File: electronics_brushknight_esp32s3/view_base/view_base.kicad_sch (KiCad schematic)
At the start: 108 parts, among them J1 BLDC, J2 USB_C_Receptacle_USB2.0, J3 LCD, J4 A, J5 B, J6 LCD - FPC, Q1 MMBT4403, Q2 UMH3N, U1 MT6701-CT, U10 ESP32-S3-WROOM-1-N8R8, U4 CP2102N-A02-GQFN28, U4 HX711, U5 TMC6300, U7 SN74LV1T34DBV, U8 VEML7700, U9 TS1117BCW33_RPG

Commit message: re-routed things
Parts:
- removed D1, D2, D3, D4, D5, D6, D7, D8: SK6812SIDE-A, cleaned footprints:SK6812-SIDE-A, symbol SK6812:SK6812SIDE-A
- removed H4: MountHole, Holes:MountingHole_2.2mm_M2_ISO7380_Pad_NonVirtual, symbol Mechanical:MountingHole_Pad
- removed Q2: UMH3N, cleaned footprints:SOT-363_SC-70-6, symbol Transistor_BJT:UMH3N
- removed R3: 1K, cleaned footprints:R_0603_1608Metric, symbol Device:R_Small
- removed U4: CP2102N-A02-GQFN28, cp2102:Silicon_Labs-CP2102N-A02-GQFN28-IPC_A, symbol terrarium-rescue:CP2102N-A02-GQFN28-CP2102N-A02-GQFN28
- added C100, C101, C30, C31, C32, C33, C34, C35, C36, C37, C38, C39, C40, C41, C42, C43, C44, C45, C46, C47, C48, C49, C50, C51, C52, C53, C54, C55, C56, C57, C58, C59, C60, C61, C62, C63, C64, C65, C66, C67, C68, C69, C70, C71, C72, C73, C74, C75, C76, C77, C79, C80, C81, C82, C88, C90, C92, C94, C95, C96, C97, C98, C99: 0.1uF, cleaned footprints:C_0402_1005Metric, symbol Device:C_Small
- added C27, C38: 10uF, smd_clean:C_0603_1608Metric, symbol Device:C_Small
- added C39: 100nF, smd_clean:C_0603_1608Metric, symbol Device:C_Small
- added D10, D11, D12, D13, D14, D15, D16, D17, D18, D19, D20, D21, D22, D23, D24, D25, D26, D27, D28, D29, D30, D31, D32, D33, D34, D35, D36, D37, D38, D39, D40, D41, D42, D43, D44, D45, D46, D47, D48, D49, D50, D51, D52, D53, D54, D55, D56, D57, D58, D59, D60, D61, D62, D63, D64, D65, D66, D67, D68, D69, D70, D71, D72, D73, D74, D75, D76, D77, D78, D79, D80, D9: SK6812, cleaned footprints:LED_SK6812_EC15_1.5x1.5mm, symbol LED:SK6812
- added Q4, Q5: BSS138, smd_clean:SOT-23, symbol Transistor_FET:BSS138
- added R18, R19, R20, R21, R22, R23: 10K, smd_clean:R_0603_1608Metric, symbol Device:R_Small
- added U2: USBLC6-2SC6, Package_TO_SOT_SMD:SOT-23-6, symbol Power_Protection:USBLC6-2SC6
- added U7: VL53L0CXV0DH_1, smd_clean:LGA12_1, symbol VL53L0CXV0DH_1:VL53L0CXV0DH_1
- added U8: LP5907MFX-2.8, Package_TO_SOT_SMD:SOT-23-5, symbol Regulator_Linear:LP5907MFX-2.8
- C1, C11, C2, C29, C3, C4, C5, C6, C7, C8: footprint cleaned footprints:C_0603_1608Metric -> cleaned footprints:C_0402_1005Metric
- TP1, TP10, TP11, TP12, TP13, TP14, TP15, TP16, TP3, TP4, TP5, TP6, TP7, TP8, TP9: footprint Modified:TestPoint_Pad_D2.0mm_ValueSilk -> cleaned footprints:TestPoint_Pad_D2.0mm_ValueSilk
- TP2: value 3.3v -> 3V3; footprint Modified:TestPoint_Pad_D2.0mm_ValueSilk -> cleaned footprints:TestPoint_Pad_D2.0mm_ValueSilk
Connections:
- net +3V3: now also C27.2, R20.2, R21.2, U8.1 (IN), U8.3 (EN); no longer C11.1
- net +5V: now also C11.1, C100.1, C101.1, C30.1, C31.1, C32.1, C33.1, C34.1, C35.1, C36.1, C37.1, C38.1, C39.1, C40.1, C41.1, C42.1, C43.1, C44.1, C45.1, C46.1, C47.1, C48.1, C49.1, C50.1, C51.1, C52.1, C53.1, C54.1, C55.1, C56.1, C57.1, C58.1, C59.1, C60.1, C61.1, C62.1, C63.1, C64.1, C65.1, C66.1, C67.1, C68.1, C69.1, C70.1, C71.1, C72.1, C73.1, C74.1, C75.1, C76.1, C77.1, C79.1, C80.1, C81.1, C82.1, C88.1, C90.1, C92.1, C94.1, C95.1, C96.1, C97.1, C98.1, C99.1, D10.3 (VDD), D11.3 (VDD), D12.3 (VDD), D13.3 (VDD), D14.3 (VDD), D15.3 (VDD), D16.3 (VDD), D17.3 (VDD), D18.3 (VDD), D19.3 (VDD), D20.3 (VDD), D21.3 (VDD), D22.3 (VDD), D23.3 (VDD), D24.3 (VDD), D25.3 (VDD), D26.3 (VDD), D27.3 (VDD), D28.3 (VDD), D29.3 (VDD), D30.3 (VDD), D31.3 (VDD), D32.3 (VDD), D33.3 (VDD), D34.3 (VDD), D35.3 (VDD), D36.3 (VDD), D37.3 (VDD), D38.3 (VDD), D39.3 (VDD), D40.3 (VDD), D41.3 (VDD), D42.3 (VDD), D43.3 (VDD), D44.3 (VDD), D45.3 (VDD), D46.3 (VDD), D47.3 (VDD), D48.3 (VDD), D49.3 (VDD), D50.3 (VDD), D51.3 (VDD), D52.3 (VDD), D53.3 (VDD), D54.3 (VDD), D55.3 (VDD), D56.3 (VDD), D57.3 (VDD), D58.3 (VDD), D59.3 (VDD), D60.3 (VDD), D61.3 (VDD), D62.3 (VDD), D63.3 (VDD), D64.3 (VDD), D65.3 (VDD), D66.3 (VDD), D67.3 (VDD), D68.3 (VDD), D69.3 (VDD), D70.3 (VDD), D71.3 (VDD), D72.3 (VDD), D73.3 (VDD), D74.3 (VDD), D75.3 (VDD), D76.3 (VDD), D77.3 (VDD), D78.3 (VDD), D79.3 (VDD), D80.3 (VDD), D9.3 (VDD), U2.5 (VBUS)
- net GND: now also C100.2, C101.2, C27.1, C30.2, C31.2, C32.2, C33.2, C34.2, C35.2, C36.2, C37.2, C38.1, C38.2, C39.1, C39.2, C40.2, C41.2, C42.2, C43.2, C44.2, C45.2, C46.2, C47.2, C48.2, C49.2, C50.2, C51.2, C52.2, C53.2, C54.2, C55.2, C56.2, C57.2, C58.2, C59.2, C60.2, C61.2, C62.2, C63.2, C64.2, C65.2, C66.2, C67.2, C68.2, C69.2, C70.2, C71.2, C72.2, C73.2, C74.2, C75.2, C76.2, C77.2, C79.2, C80.2, C81.2, C82.2, C88.2, C90.2, C92.2, C94.2, C95.2, C96.2, C97.2, C98.2, C99.2, D10.1 (VSS), D11.1 (VSS), D12.1 (VSS), D13.1 (VSS), D14.1 (VSS), D15.1 (VSS), D16.1 (VSS), D17.1 (VSS), D18.1 (VSS), D19.1 (VSS), D20.1 (VSS), D21.1 (VSS), D22.1 (VSS), D23.1 (VSS), D24.1 (VSS), D25.1 (VSS), D26.1 (VSS), D27.1 (VSS), D28.1 (VSS), D29.1 (VSS), D30.1 (VSS), D31.1 (VSS), D32.1 (VSS), D33.1 (VSS), D34.1 (VSS), D35.1 (VSS), D36.1 (VSS), D37.1 (VSS), D38.1 (VSS), D39.1 (VSS), D40.1 (VSS), D41.1 (VSS), D42.1 (VSS), D43.1 (VSS), D44.1 (VSS), D45.1 (VSS), D46.1 (VSS), D47.1 (VSS), D48.1 (VSS), D49.1 (VSS), D50.1 (VSS), D51.1 (VSS), D52.1 (VSS), D53.1 (VSS), D54.1 (VSS), D55.1 (VSS), D56.1 (VSS), D57.1 (VSS), D58.1 (VSS), D59.1 (VSS), D60.1 (VSS), D61.1 (VSS), D62.1 (VSS), D63.1 (VSS), D64.1 (VSS), D65.1 (VSS), D66.1 (VSS), D67.1 (VSS), D68.1 (VSS), D69.1 (VSS), D70.1 (VSS), D71.1 (VSS), D72.1 (VSS), D73.1 (VSS), D74.1 (VSS), D75.1 (VSS), D76.1 (VSS), D77.1 (VSS), D78.1 (VSS), D79.1 (VSS), D80.1 (VSS), D9.1 (VSS), U2.2 (GND), U7.12 (GND4), U7.2 (AVSSVCSEL), U7.3 (GND), U7.4 (GND2), U7.6 (GND3), U8.2 (GND)
- net LCD_RST: now also U10.18 (IO10); no longer U10.6 (IO6)
- net LED_DATA_3V3: now also U10.20 (IO12); no longer U10.7 (IO7)
- net LED_DATA_5V: now also D9.2 (DIN)
- net MAG_CSN: now also U10.19 (IO11); no longer U10.22 (IO14)
- net MAG_DO: now also U10.22 (IO14); no longer U10.30 (IO37)
- net SCL: now also U10.31 (IO38), Q4.3 (D), R21.1; no longer U10.12 (IO8)
- net SDA: now also U10.32 (IO39), Q5.3 (D), R20.1; no longer U10.8 (IO15)
- net STRAIN_DO: now also U10.23 (IO21); no longer U10.31 (IO38)
- net TMC_DIAG: now also U10.6 (IO6); no longer U10.29 (IO36)
- net TMC_UH: now also U10.12 (IO8); no longer U10.14 (IO20)
- net TMC_UL: now also U10.9 (IO16); no longer U10.13 (IO19)
- net TMC_VH: now also U10.11 (IO18); no longer U10.23 (IO21)
- net TMC_VL: now also U10.7 (IO7); no longer U10.10 (IO17)
- net TMC_WH: now also U10.10 (IO17); no longer U10.20 (IO12)
- net TMC_WL: now also U10.8 (IO15); no longer U10.11 (IO18)
- net USB_D+: now also U2.3 (I/O2)
- net USB_D-: now also U2.1 (I/O1)
- new net: D27.4 (DOUT), D28.2 (DIN)
- new net: D28.4 (DOUT), D29.2 (DIN)
- new net: D19.4 (DOUT), D20.2 (DIN)
- new net: D20.4 (DOUT), D21.2 (DIN)
- new net: D16.4 (DOUT), D17.2 (DIN)
- new net: D17.4 (DOUT), D18.2 (DIN)
- new net: D34.4 (DOUT), D35.2 (DIN)
- new net: D35.4 (DOUT), D36.2 (DIN)
- new net: D36.4 (DOUT), D37.2 (DIN)
- new net: R19.1, U7.7 (GPIO1)
- new net: D48.4 (DOUT), D52.2 (DIN)
- new net: D52.4 (DOUT), D56.2 (DIN)
- new net: D59.4 (DOUT), D63.2 (DIN)
- new net: D63.4 (DOUT), D67.2 (DIN)
- new net: R18.1, U7.5 (XSHUT)
- new net: D40.4 (DOUT), D41.2 (DIN)
- new net: D41.4 (DOUT), D45.2 (DIN)
- new net: D74.4 (DOUT), D75.2 (DIN)
- new net: D75.4 (DOUT), D76.2 (DIN)
- new net: D24.4 (DOUT), D25.2 (DIN)
- new net: D25.4 (DOUT), D26.2 (DIN)
- new net: D64.4 (DOUT), D68.2 (DIN)
- new net: D68.4 (DOUT), D72.2 (DIN)
- new net: D56.4 (DOUT), D60.2 (DIN)
- new net: D60.4 (DOUT), D64.2 (DIN)
- new net: D49.4 (DOUT), D53.2 (DIN)
- new net: D53.4 (DOUT), D57.2 (DIN)
- new net: D12.4 (DOUT), D13.2 (DIN)
- new net: D13.4 (DOUT), D14.2 (DIN)
- new net: D14.4 (DOUT), D15.2 (DIN)
- new net: D15.4 (DOUT), D16.2 (DIN)
- new net: D61.4 (DOUT), D65.2 (DIN)
- new net: D65.4 (DOUT), D69.2 (DIN)
- new net: D67.4 (DOUT), D71.2 (DIN)
- new net: D44.2 (DIN), D71.4 (DOUT)
- new net: D18.4 (DOUT), D19.2 (DIN)
- new net: D76.4 (DOUT), D77.2 (DIN)
- new net: D77.4 (DOUT), D78.2 (DIN)
- new net: D42.2 (DIN), D69.4 (DOUT)
- new net: D42.4 (DOUT), D46.2 (DIN)
- new net: D46.4 (DOUT), D50.2 (DIN)
- new net: D50.4 (DOUT), D54.2 (DIN)
- new net: D30.4 (DOUT), D31.2 (DIN)
- new net: D31.4 (DOUT), D32.2 (DIN)
- new net: D55.4 (DOUT), D59.2 (DIN)
- new net: D33.4 (DOUT), D34.2 (DIN)
- new net: D26.4 (DOUT), D27.2 (DIN)
- new net: D21.4 (DOUT), D22.2 (DIN)
- new net: D22.4 (DOUT), D23.2 (DIN)
- new net: D44.4 (DOUT), D48.2 (DIN)
- new net: D23.4 (DOUT), D24.2 (DIN)
- new net: D29.4 (DOUT), D30.2 (DIN)
- new net: D78.4 (DOUT), D79.2 (DIN)
- new net: D79.4 (DOUT), D80.2 (DIN)
- new net: D43.4 (DOUT), D47.2 (DIN)
- new net: D47.4 (DOUT), D51.2 (DIN)
- new net: D32.4 (DOUT), D33.2 (DIN)
- new net: D58.4 (DOUT), D62.2 (DIN)
- new net: D62.4 (DOUT), D66.2 (DIN)
- new net: D73.4 (DOUT), D74.2 (DIN)
- new net: D72.4 (DOUT), D73.2 (DIN)
- new net: D43.2 (DIN), D70.4 (DOUT)
- new net: D57.4 (DOUT), D61.2 (DIN)
- new net: D37.4 (DOUT), D38.2 (DIN)
- new net: D39.4 (DOUT), D40.2 (DIN)
- new net: D45.4 (DOUT), D49.2 (DIN)
- new net: D38.4 (DOUT), D39.2 (DIN)
- new net: D66.4 (DOUT), D70.2 (DIN)
- new net: D11.4 (DOUT), D12.2 (DIN)
- new net: D54.4 (DOUT), D58.2 (DIN)
- new net: D10.4 (DOUT), D11.2 (DIN)
- new net: D51.4 (DOUT), D55.2 (DIN)
- new net: D10.2 (DIN), D9.4 (DOUT)
- new net +2V8: C38.2, C39.2, Q4.1 (G), Q5.1 (G), R18.2, R19.2, R22.2, R23.2, U7.1 (AVDDVCSEL), U7.11 (AVDD), U8.5 (OUT)
- new net ESP_USB_D+: U10.14 (IO20), U2.4 (I/O2)
- new net ESP_USB_D-: U10.13 (IO19), U2.6 (I/O1)
- new net SCL_2.8: Q4.2 (S), R23.1, U7.10 (SCL)
- new net SDA_2.8: Q5.2 (S), R22.1, U7.9 (SDA)
- no-connect marks 32 -> 19
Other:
- note added: "Level shifter & pull-ups (Proximity sensor)"
- note added: "Power supply (Proximity sensor)"
- note added: "Proximity sensor"
- note removed: "Reset/Boot via USB serial"

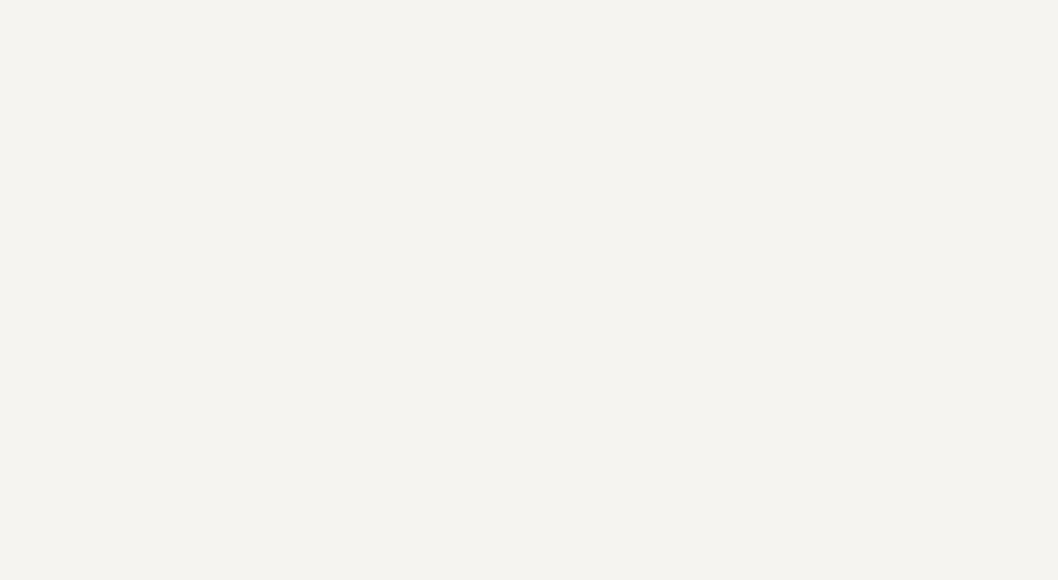
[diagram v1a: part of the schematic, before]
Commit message: updated screen PCB
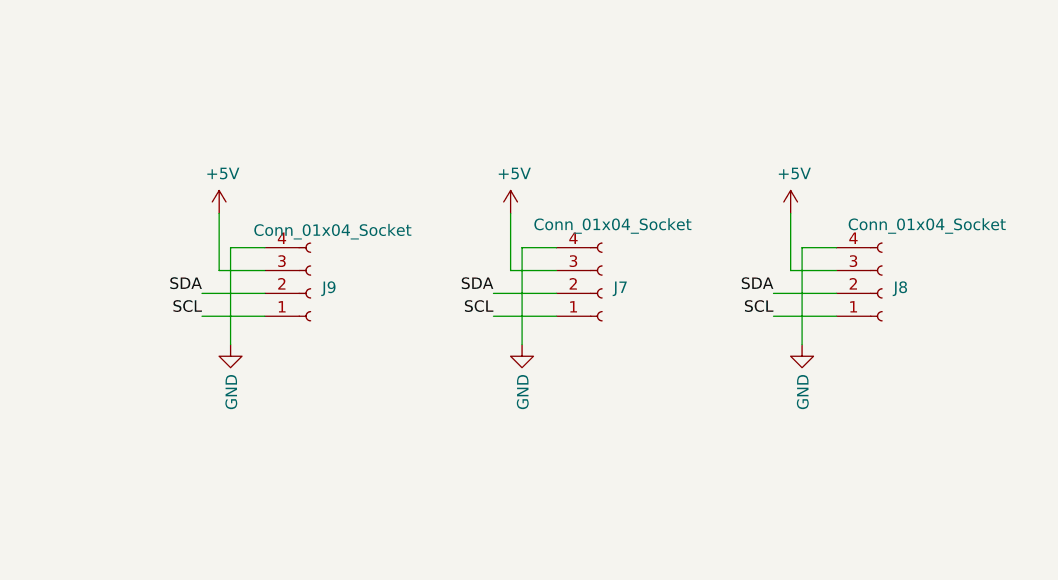
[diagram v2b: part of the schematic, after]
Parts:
- added J7, J8, J9: Conn_01x04_Socket, cleaned footprints:JST_SH_SM04B-SRSS-TB_1x04-1MP_P1.00mm_Horizontal, symbol Connector:Conn_01x04_Socket
- U2: footprint Package_TO_SOT_SMD:SOT-23-6 -> smd_clean:SOT-23-6
- U8: footprint Package_TO_SOT_SMD:SOT-23-5 -> cleaned footprints:SOT-23-5
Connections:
- net +5V: now also J7.3 (Pin_3), J8.3 (Pin_3), J9.3 (Pin_3)
- net GND: now also J7.4 (Pin_4), J8.4 (Pin_4), J9.4 (Pin_4)
- net SCL: now also J7.1 (Pin_1), J8.1 (Pin_1), J9.1 (Pin_1)
- net SDA: now also J7.2 (Pin_2), J8.2 (Pin_2), J9.2 (Pin_2)

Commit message: run DRC
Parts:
- added R28: 10k, cleaned footprints:R_0603_1608Metric, symbol Device:R_Small
- added SW1: RST, smd_clean:SW_SPST_PTS810, symbol Switch:SW_Push
- added SW2: Boot, smd_clean:SW_SPST_PTS810, symbol Switch:SW_Push
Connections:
- net +3V3: now also R28.1
- net ESP32_BOOT: now also R28.2, SW2.1
- net ESP32_EN: now also SW1.1
- net GND: now also SW1.2, SW2.2
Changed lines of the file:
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@@
   (junction (at 195.58 483.235) (diameter 0) (color 0 0 0 0)
   )
+  (junction (at 241.3 139.7) (diameter 0) (color 0 0 0 0)
+  )
   (junction (at 255.27 376.555) (diameter 0) (color 0 0 0 0)
   )
@@
   (junction (at 82.55 323.215) (diameter 0) (color 0 0 0 0)
   )
+  (junction (at 314.325 127) (diameter 0) (color 0 0 0 0)
+  )
   (junction (at 127 168.91) (diameter 0) (color 0 0 0 0)
   )
@@
     (stroke (width 0) (type default))
   )
+  (wire (pts (xy 292.735 127) (xy 314.325 127))
+    (stroke (width 0) (type default))
+  )
   (wire (pts (xy 422.275 332.74) (xy 417.195 332.74))
     (stroke (width 0) (type default))
@@
     (stroke (width 0) (type default))
   )
+  (wire (pts (xy 314.325 127) (xy 314.325 124.46))
+    (stroke (width 0) (type default))
+  )
   (wire (pts (xy 497.205 350.52) (xy 497.205 354.965))
     (stroke (width 0) (type default))
@@
     (stroke (width 0) (type default))
   )
+  (wire (pts (xy 251.46 133.35) (xy 251.46 139.7))
+    (stroke (width 0) (type default))
+  )
   (wire (pts (xy 137.795 405.13) (xy 137.795 415.29))
     (stroke (width 0) (type default))
@@
     (stroke (width 0) (type default))
   )
+  (wire (pts (xy 314.325 119.38) (xy 314.325 116.84))
+    (stroke (width 0) (type default))
+  )
   (wire (pts (xy 45.72 137.16) (xy 45.72 134.62))
     (stroke (width 0) (type default))
@@
     (stroke (width 0) (type default))
   )
+  (wire (pts (xy 324.485 133.35) (xy 314.325 133.35))
+    (stroke (width 0) (type default))
+  )
   (wire (pts (xy 109.22 339.09) (xy 117.475 339.09))
     (stroke (width 0) (type default))
@@
     (stroke (width 0) (type default))
   )
+  (wire (pts (xy 251.46 139.7) (xy 241.3 139.7))
+    (stroke (width 0) (type default))
+  )
   (wire (pts (xy 388.62 28.575) (xy 394.97 28.575))
     (stroke (width 0) (type default))
@@
     (stroke (width 0) (type default))
   )
+  (wire (pts (xy 324.485 127) (xy 324.485 133.35))
+    (stroke (width 0) (type default))
+  )
   (wire (pts (xy 105.41 74.93) (xy 103.505 74.93))
     (stroke (width 0) (type default))
@@
     (stroke (width 0) (type default))
   )
+  (wire (pts (xy 314.325 134.62) (xy 314.325 133.35))
+    (stroke (width 0) (type default))
+  )
   (wire (pts (xy 255.27 354.33) (xy 266.065 354.33))
     (stroke (width 0) (type default))
@@
     (effects (font (size 1.27 1.27)) (justify right bottom))
   )
+  (label "ESP32_BOOT" (at 292.735 127 0) (fields_autoplaced)
+    (effects (font (size 1.27 1.27)) (justify left bottom))
+  )
   (label "STRAIN_S+" (at 121.92 189.23 0) (fields_autoplaced)
     (effects (font (size 1.27 1.27)) (justify left bottom))
@@
     )
   )
+  (symbol (lib_id "Device:R_Small") (at 314.325 121.92 0) (unit 1)
+    (in_bom yes) (on_board yes) (dnp no)
+    (property "Reference" "R28" (at 309.3466 121.92 90)
+      (effects (font (size 1.27 1.27)))
+    )
+    (property "Value" "10k" (at 311.658 121.92 90)
+      (effects (font (size 1.27 1.27)))
+    )
+    (property "Footprint" "cleaned footprints:R_0603_1608Metric" (at 314.325 121.92 0)
+      (effects (font (size 1.27 1.27)) hide)
+    )
+    (property "Datasheet" "~" (at 314.325 121.92 0)
+      (effects (font (size 1.27 1.27)) hide)
+    )
+    (property "LCSC" "C98220" (at 314.325 121.92 0)
+      (effects (font (size 1.27 1.27)) hide)
+    )
+    (property "Digikey" "RMCF0603JT10K0CT-ND" (at 314.325 121.92 0)
+      (effects (font (size 1.27 1.27)) hide)
+    )
+    (property "Mouser" "652-CR0603FX-1002ELF" (at 314.325 121.92 0)
+      (effects (font (size 1.27 1.27)) hide)
+    )
+    (pin "1")
+    (pin "2")
+    (instances
+      (project "view_base"
+        (path "/5edcefbe-9766-42c8-9529-28d0ec865573"
+          (reference "R28") (unit 1)
+        )
+      )
+    )
+  )
   (symbol (lib_id "LED:SK6812") (at 101.6 315.595 0) (unit 1)
     (in_bom yes) (on_board yes) (dnp no)
@@
     )
   )
+  (symbol (lib_id "Switch:SW_Push") (at 319.405 127 0) (unit 1)
+    (in_bom yes) (on_board yes) (dnp no) (fields_autoplaced)
+    (property "Reference" "SW2" (at 319.405 120.65 0)
+      (effects (font (size 1.27 1.27)))
+    )
+    (property "Value" "Boot" (at 319.405 123.19 0)
+      (effects (font (size 1.27 1.27)))
+    )
+    (property "Footprint" "smd_clean:SW_SPST_PTS810" (at 319.405 121.92 0)
+      (effects (font (size 1.27 1.27)) hide)
+    )
+    (property "Datasheet" "~" (at 319.405 121.92 0)
+      (effects (font (size 1.27 1.27)) hide)
+    )
+    (pin "1")
+    (pin "2")
+    (instances
+      (project "view_base"
+        (path "/5edcefbe-9766-42c8-9529-28d0ec865573"
+          (reference "SW2") (unit 1)
+        )
+      )
+    )
+  )
   (symbol (lib_id "LED:SK6812") (at 219.075 431.165 0) (unit 1)
     (in_bom yes) (on_board yes) (dnp no)
@@
     )
   )
+  (symbol (lib_id "power:GND") (at 314.325 134.62 0) (unit 1)
+    (in_bom yes) (on_board yes) (dnp no)
+    (property "Reference" "#PWR031" (at 314.325 140.97 0)
+      (effects (font (size 1.27 1.27)) hide)
+    )
+    (property "Value" "GND" (at 314.452 139.0142 0)
+      (effects (font (size 1.27 1.27)))
+    )
+    (property "Footprint" "" (at 314.325 134.62 0)
+      (effects (font (size 1.27 1.27)) hide)
+    )
+    (property "Datasheet" "" (at 314.325 134.62 0)
+      (effects (font (size 1.27 1.27)) hide)
+    )
+    (pin "1")
+    (instances
+      (project "view_base"
+        (path "/5edcefbe-9766-42c8-9529-28d0ec865573"
+          (reference "#PWR031") (unit 1)
+        )
+      )
+    )
+  )
   (symbol (lib_id "Device:C_Small") (at 137.795 334.01 0) (unit 1)
     (in_bom yes) (on_board yes) (dnp no)
@@
     )
   )
+  (symbol (lib_id "power:+3.3V") (at 314.325 116.84 0) (unit 1)
+    (in_bom yes) (on_board yes) (dnp no)
+    (property "Reference" "#PWR030" (at 314.325 120.65 0)
+      (effects (font (size 1.27 1.27)) hide)
+    )
+    (property "Value" "+3.3V" (at 314.706 112.4458 0)
+      (effects (font (size 1.27 1.27)))
+    )
+    (property "Footprint" "" (at 314.325 116.84 0)
+      (effects (font (size 1.27 1.27)) hide)
+    )
+    (property "Datasheet" "" (at 314.325 116.84 0)
+      (effects (font (size 1.27 1.27)) hide)
+    )
+    (pin "1")
+    (instances
+      (project "view_base"
+        (path "/5edcefbe-9766-42c8-9529-28d0ec865573"
+          (reference "#PWR030") (unit 1)
+        )
+      )
+    )
+  )
   (symbol (lib_id "LED:SK6812") (at 219.075 384.175 0) (unit 1)
     (in_bom yes) (on_board yes) (dnp no)
@@
         )
       )
+    )
+  )
+  (symbol (lib_id "Switch:SW_Push") (at 246.38 133.35 0) (unit 1)
+    (in_bom yes) (on_board yes) (dnp no) (fields_autoplaced)
+    (property "Reference" "SW1" (at 246.38 127 0)
+      (effects (font (size 1.27 1.27)))
+    )
+    (property "Value" "RST" (at 246.38 129.54 0)
+      (effects (font (size 1.27 1.27)))
+    )
+    (property "Footprint" "smd_clean:SW_SPST_PTS810" (at 246.38 128.27 0)
+      (effects (font (size 1.27 1.27)) hide)
+    )
+    (property "Datasheet" "~" (at 246.38 128.27 0)
+      (effects (font (size 1.27 1.27)) hide)
+    )
+    (pin "1")
+    (pin "2")
+    (instances
+      (project "view_base"
+        (path "/5edcefbe-9766-42c8-9529-28d0ec865573"
+          (reference "SW1") (unit 1)
+        )
+      )
